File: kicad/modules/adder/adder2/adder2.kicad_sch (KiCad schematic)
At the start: 6 parts, among them U3301 74HC86

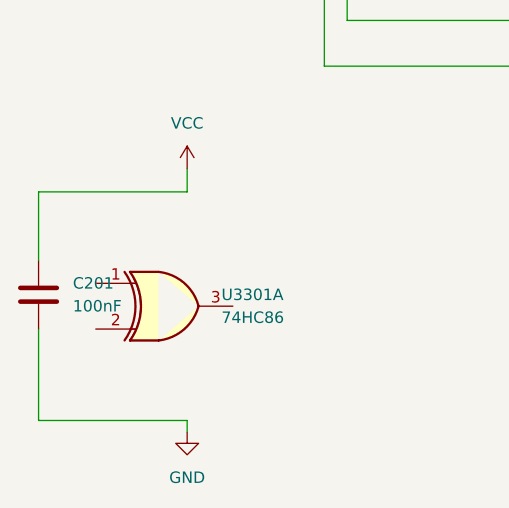
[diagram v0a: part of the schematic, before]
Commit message: Fix KiCad file paths and complete core circuit design
- Fixed file path errors across all KiCad schematics and projects
- Completed core circuit designs:
  * Adder and subtractor modules (adder2, adder8)
  * LED panels (led_panel_1) with display circuits
  * Flag LED circuits for status indicators
  * All dependent logic gate modules (AND, OR, NOT, NAND, NOR, XOR)
  * All multiplexer modules (2:1, 4:1, 8:1, 8-bit)
  * Main control board schematics
  * Flags board schematics
- Updated .gitignore to exclude KiCad backups, cache files, and lock files
- Ready for pin placement and routing of control buses, power rails, and inter-board signals
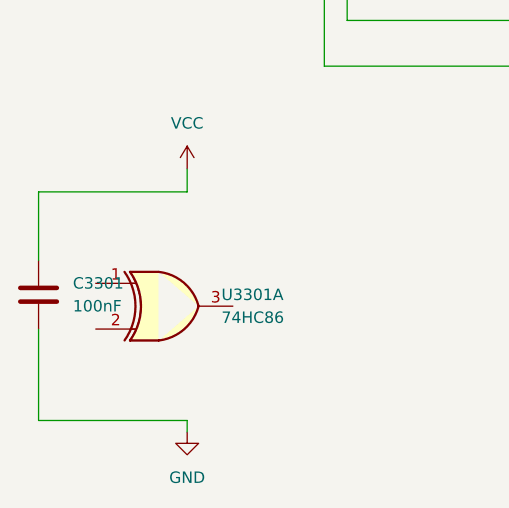
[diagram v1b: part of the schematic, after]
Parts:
- renumbered C201 to C3301
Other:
- sheet or2_1: file ../../modules/gates/gate_or/gate_or_2in/gate_or_2in.kicad_sch -> ../../gates/gate_or/gate_or_2in/gate_or_2in.kicad_sch
- sheet or2_2: file ../../modules/gates/gate_or/gate_or_2in/gate_or_2in.kicad_sch -> ../../gates/gate_or/gate_or_2in/gate_or_2in.kicad_sch
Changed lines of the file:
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@@
 		(dnp no)
 		(fields_autoplaced yes)
-		(property "Reference" "C201"
+		(property "Reference" "C?"
 			(at 24.13 144.7799 0)
 			(effects
@@
 				(path "/1a086df7-7508-4c0d-b696-2f052ea4c322/92236a5d-2e44-4e21-b0a9-9f7c8d85dee0/e678a1db-fc7f-4871-8288-df3fa647bce0"
 					(reference "C2201")
+					(unit 1)
+				)
+			)
+			(project "adder2"
+				(path "/e938a6bb-35cc-48f7-b2cb-f9f5c6ada261"
+					(reference "C?")
 					(unit 1)
 				)
@@
 				)
 				(path "/1a086df7-7508-4c0d-b696-2f052ea4c322/92236a5d-2e44-4e21-b0a9-9f7c8d85dee0/5ca3f5ef-5ebe-454d-ad68-04b74d36a9c7"
-					(reference "U?")
+					(reference "U204")
 					(unit 1)
 				)
@@
 					(reference "U2201")
 					(unit 2)
+				)
+			)
+			(project "adder2"
+				(path "/e938a6bb-35cc-48f7-b2cb-f9f5c6ada261"
+					(reference "U?")
+					(unit 1)
 				)
 			)
@@
 				)
 				(path "/1a086df7-7508-4c0d-b696-2f052ea4c322/92236a5d-2e44-4e21-b0a9-9f7c8d85dee0/5ca3f5ef-5ebe-454d-ad68-04b74d36a9c7"
-					(reference "U?")
+					(reference "U201")
 					(unit 1)
 				)
@@
 					(reference "U2201")
 					(unit 5)
+				)
+			)
+			(project "adder2"
+				(path "/e938a6bb-35cc-48f7-b2cb-f9f5c6ada261"
+					(reference "U?")
+					(unit 1)
 				)
 			)
@@
 				)
 				(path "/1a086df7-7508-4c0d-b696-2f052ea4c322/92236a5d-2e44-4e21-b0a9-9f7c8d85dee0/5ca3f5ef-5ebe-454d-ad68-04b74d36a9c7"
-					(reference "U?")
+					(reference "U203")
 					(unit 1)
 				)
@@
 					(reference "U2201")
 					(unit 3)
+				)
+			)
+			(project "adder2"
+				(path "/e938a6bb-35cc-48f7-b2cb-f9f5c6ada261"
+					(reference "U?")
+					(unit 1)
 				)
 			)
@@
 				)
 				(path "/1a086df7-7508-4c0d-b696-2f052ea4c322/92236a5d-2e44-4e21-b0a9-9f7c8d85dee0/5ca3f5ef-5ebe-454d-ad68-04b74d36a9c7"
-					(reference "U?")
+					(reference "U205")
 					(unit 1)
 				)
@@
 					(reference "U2201")
 					(unit 4)
+				)
+			)
+			(project "adder2"
+				(path "/e938a6bb-35cc-48f7-b2cb-f9f5c6ada261"
+					(reference "U?")
+					(unit 1)
 				)
 			)
@@
 		(dnp no)
 		(fields_autoplaced yes)
-		(property "Reference" "#PWR0202"
+		(property "Reference" "#PWR?"
 			(at 36.83 167.64 0)
 			(effects
@@
 				(path "/1a086df7-7508-4c0d-b696-2f052ea4c322/92236a5d-2e44-4e21-b0a9-9f7c8d85dee0/e678a1db-fc7f-4871-8288-df3fa647bce0"
 					(reference "#PWR02202")
+					(unit 1)
+				)
+			)
+			(project "adder2"
+				(path "/e938a6bb-35cc-48f7-b2cb-f9f5c6ada261"
+					(reference "#PWR?")
 					(unit 1)
 				)
@@
 				)
 				(path "/1a086df7-7508-4c0d-b696-2f052ea4c322/92236a5d-2e44-4e21-b0a9-9f7c8d85dee0/5ca3f5ef-5ebe-454d-ad68-04b74d36a9c7"
-					(reference "U?")
+					(reference "U202")
 					(unit 1)
 				)
 				(path "/1a086df7-7508-4c0d-b696-2f052ea4c322/92236a5d-2e44-4e21-b0a9-9f7c8d85dee0/e678a1db-fc7f-4871-8288-df3fa647bce0"
 					(reference "U2201")
+					(unit 1)
+				)
+			)
+			(project "adder2"
+				(path "/e938a6bb-35cc-48f7-b2cb-f9f5c6ada261"
+					(reference "U?")
 					(unit 1)
 				)
@@
 		(dnp no)
 		(fields_autoplaced yes)
-		(property "Reference" "#PWR0201"
+		(property "Reference" "#PWR?"
 			(at 36.83 135.89 0)
 			(effects
@@
 				(path "/1a086df7-7508-4c0d-b696-2f052ea4c322/92236a5d-2e44-4e21-b0a9-9f7c8d85dee0/e678a1db-fc7f-4871-8288-df3fa647bce0"
 					(reference "#PWR02201")
+					(unit 1)
+				)
+			)
+			(project "adder2"
+				(path "/e938a6bb-35cc-48f7-b2cb-f9f5c6ada261"
+					(reference "#PWR?")
 					(unit 1)
 				)
@@
 				)
 			)
+			(project "adder2"
+				(path "/e938a6bb-35cc-48f7-b2cb-f9f5c6ada261"
+					(page "2")
+				)
+			)
 		)
 	)
@@
 			)
 		)
-		(property "Sheetfile" "../../modules/gates/gate_or/gate_or_2in/gate_or_2in.kicad_sch"
+		(property "Sheetfile" "../../gates/gate_or/gate_or_2in/gate_or_2in.kicad_sch"
 			(at 110.49 58.3696 0)
 			(effects
@@
 				(path "/1a086df7-7508-4c0d-b696-2f052ea4c322/92236a5d-2e44-4e21-b0a9-9f7c8d85dee0/072d980d-7920-4601-abce-27648096a13e"
 					(page "41")
+				)
+			)
+			(project "adder2"
+				(path "/e938a6bb-35cc-48f7-b2cb-f9f5c6ada261"
+					(page "10")
 				)
 			)
@@
 				)
 			)
+			(project "adder2"
+				(path "/e938a6bb-35cc-48f7-b2cb-f9f5c6ada261"
+					(page "8")
+				)
+			)
 		)
 	)
@@
 				)
 			)
+			(project "adder2"
+				(path "/e938a6bb-35cc-48f7-b2cb-f9f5c6ada261"
+					(page "4")
+				)
+			)
 		)
 	)
@@
 				)
 			)
+			(project "adder2"
+				(path "/e938a6bb-35cc-48f7-b2cb-f9f5c6ada261"
+					(page "6")
+				)
+			)
 		)
 	)
@@
 			)
 		)
-		(property "Sheetfile" "../../modules/gates/gate_or/gate_or_2in/gate_or_2in.kicad_sch"
+		(property "Sheetfile" "../../gates/gate_or/gate_or_2in/gate_or_2in.kicad_sch"
 			(at 127 118.0596 0)
 			(effects
@@
 		)
 		(instances
-			(project "add_sub"
-				(path "/1a086df7-7508-4c0d-b696-2f052ea4c322/92236a5d-2e44-4e21-b0a9-9f7c8d85dee0/5ca3f5ef-5ebe-454d-ad68-04b74d36a9c7"
-					(page "8")
-				)
-				(path "/1a086df7-7508-4c0d-b696-2f052ea4c322/92236a5d-2e44-4e21-b0a9-9f7c8d85dee0/0a1186b3-be7e-452c-80fb-048fb270c396"
-					(page "16")
-				)
-				(path "/1a086df7-7508-4c0d-b696-2f052ea4c322/92236a5d-2e44-4e21-b0a9-9f7c8d85dee0/e678a1db-fc7f-4871-8288-df3fa647bce0"
-					(page "27")
-				)
-				(path "/1a086df7-7508-4c0d-b696-2f052ea4c322/92236a5d-2e44-4e21-b0a9-9f7c8d85dee0/072d980d-7920-4601-abce-27648096a13e"
-					(page "38")
-				)
-			)
-		)
-	)
+			(project "adder2"
+				(path "/e938a6bb-35cc-48f7-b2cb-f9f5c6ada261"
+					(page "11")
+				)
+			)
+		)
+	)
+	(sheet_instances
+		(path "/"
+			(page "1")
+		)
+	)
+	(embedded_fonts no)
 )
